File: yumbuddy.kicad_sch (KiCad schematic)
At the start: 26 parts, among them P1 USB_C_Plug_USB2.0, SW1 SW_MEC_5E, SW2 SW_MEC_5E, U1 ESP32-C6FH4

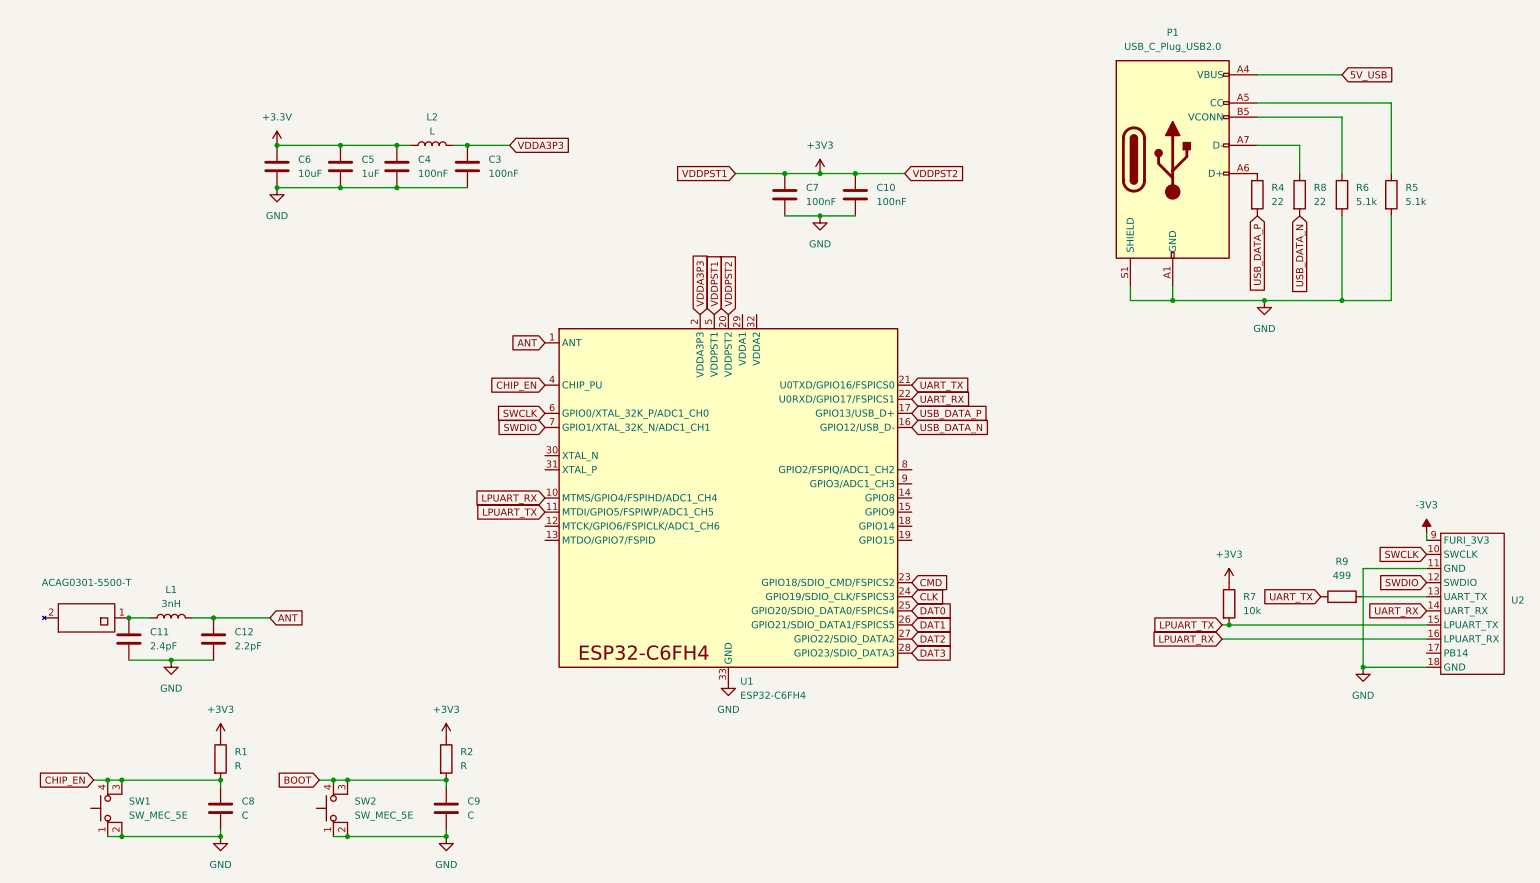
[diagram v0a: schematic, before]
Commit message: component footprint and mapping, update schematics
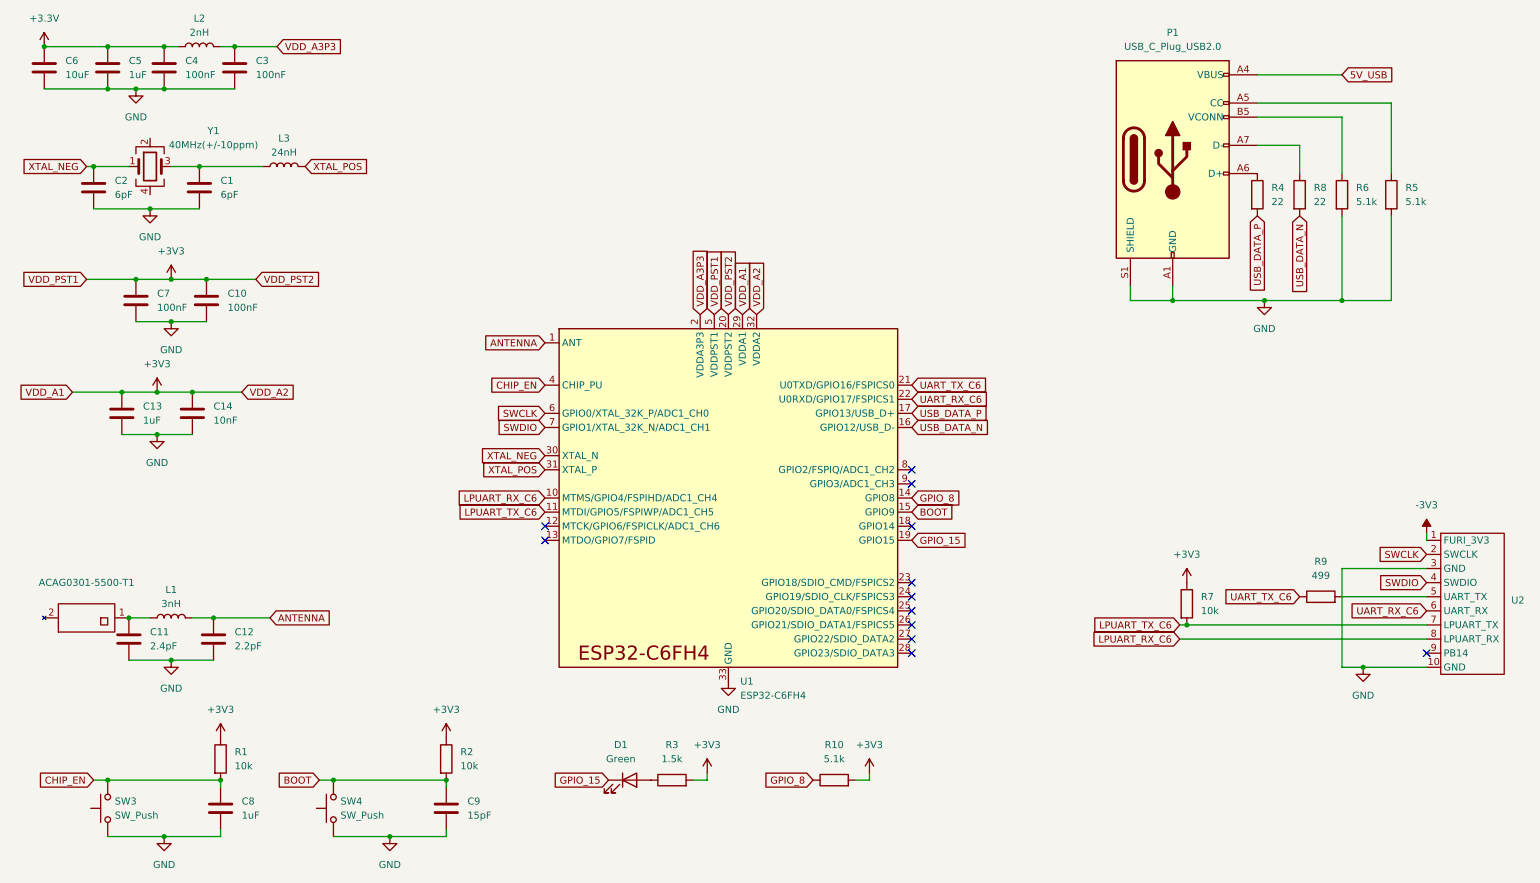
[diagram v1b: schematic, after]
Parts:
- removed SW1, SW2: SW_MEC_5E, symbol Switch:SW_MEC_5E
- added C1, C2: 6pF, Resistor_SMD:R_0603_1608Metric, symbol Device:C
- added C13: 1uF, Resistor_SMD:R_0603_1608Metric, symbol Device:C
- added C14: 10nF, Resistor_SMD:R_0603_1608Metric, symbol Device:C
- added D1: Green, LED_SMD:LED_0603_1608Metric, symbol Device:LED
- added L3: 24nH, Inductor_SMD:L_0603_1608Metric, symbol Device:L
- added R10: 5.1k, Resistor_SMD:R_0603_1608Metric, symbol Device:R
- added R3: 1.5k, Resistor_SMD:R_0603_1608Metric, symbol Device:R
- added SW3, SW4: SW_Push, Button_Switch_SMD:SW_Push_SPST_NO_Alps_SKRK, symbol Switch:SW_Push
- added Y1: 40MHz(+/-10ppm), Crystal:Crystal_SMD_1210-4Pin_1.2x1.0mm, symbol Device:Crystal_GND24
- ACAG0301-5500-T1: renamed from ACAG0301-5500-T; footprint (none) -> RF_Antenna:Johanson_2450AT43F0100
- C10, C11, C12, C3, C4, C5, C6, C7, R4, R5, R6, R7, R8, R9: footprint (none) -> Resistor_SMD:R_0603_1608Metric
- C8: value C -> 1uF; footprint (none) -> Resistor_SMD:R_0603_1608Metric
- C9: value C -> 15pF; footprint (none) -> Resistor_SMD:R_0603_1608Metric
- L1: footprint (none) -> Inductor_SMD:L_0603_1608Metric
- L2: value L -> 2nH; footprint (none) -> Inductor_SMD:L_0603_1608Metric
- P1: footprint (none) -> Connector_USB:USB_C_Receptacle_Amphenol_124019772112A
- R1, R2: value R -> 10k; footprint (none) -> Resistor_SMD:R_0603_1608Metric
- U2: footprint (none) -> Connector_PinHeader_2.54mm:PinHeader_1x10_P2.54mm_Horizontal
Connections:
- net +3V3: now also U1.29 (VDDA1), U1.32 (VDDA2), C13.1, C14.1, R10.2, R3.2
- net -3V3: now also U2.1 (FURI_3V3); no longer U2.9 (FURI_3V3)
- net BOOT: now also U1.15 (GPIO9), SW4.2
- net CHIP_EN: now also SW3.2
- net GND: now also U2.10 (GND), U2.3 (GND), C1.2, C13.2, C14.2, C2.2, SW3.1, SW4.1; no longer U2.11 (GND), U2.18 (GND)
- net SWCLK: now also U2.2 (SWCLK); no longer U2.10 (SWCLK)
- net SWDIO: now also U2.4 (SWDIO); no longer U2.12 (SWDIO)
- net at R9.2: now also U2.5 (UART_TX); no longer U2.13 (UART_TX)
- net GPIO_8: now reaches U1.14 (GPIO8)
- net GPIO_8: now also R10.1
- net GPIO_15: now reaches U1.19 (GPIO15)
- net GPIO_15: now also D1.1 (K)
- net XTAL_NEG: now reaches U1.30 (XTAL_N)
- net XTAL_NEG: now also C2.1, Y1.1
- net XTAL_POS: now reaches U1.31 (XTAL_P)
- net XTAL_POS: now also L3.2
- net ANT renamed ANTENNA
- net CLK: no longer names the net of U1.24 (GPIO19/SDIO_CLK/FSPICS3)
- net CMD: no longer names the net of U1.23 (GPIO18/SDIO_CMD/FSPICS2)
- net DAT0: no longer names the net of U1.25 (GPIO20/SDIO_DATA0/FSPICS4)
- net DAT1: no longer names the net of U1.26 (GPIO21/SDIO_DATA1/FSPICS5)
- net DAT2: no longer names the net of U1.27 (GPIO22/SDIO_DATA2)
- net DAT3: no longer names the net of U1.28 (GPIO23/SDIO_DATA3)
- net LPUART_RX renamed LPUART_RX_C6
- net LPUART_RX_C6: now also U2.8 (LPUART_RX); no longer U2.16 (LPUART_RX)
- net LPUART_TX renamed LPUART_TX_C6
- net LPUART_TX_C6: now also U2.7 (LPUART_TX); no longer U2.15 (LPUART_TX)
- net UART_RX renamed UART_RX_C6
- net UART_RX_C6: now also U2.6 (UART_RX); no longer U2.14 (UART_RX)
- net UART_TX renamed UART_TX_C6
- net VDDA3P3 renamed VDD_A3P3
- new net: C1.1, L3.1, Y1.3
- new net: D1.2 (A), R3.1
- no-connect marks 0 -> 12
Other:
- moved on the sheet: C10, C3, C4, C5, C6, C7, L2, R7, R9
